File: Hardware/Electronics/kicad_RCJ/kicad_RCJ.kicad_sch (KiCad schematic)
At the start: 79 parts, among them J1 Raspberry_Pi_2_3, J10 Conn_01x04_M1_extra, J11 Conn_01x04_M2_extra, J12 Conn_01x04_M3_extra, J13 Conn_01x04_M4_extra, J14 Conn_01x06_teensy_left_extra, J15 Conn_01x04_teensy_right_extra, J16 Conn_01x07_IO_expander_extra, J17 Conn_02x03_I2C, J18 Conn_02x05_3V3_GND, J19 Conn_02x05_5V_GND, J2 Conn_01x06_IMU_extra, J20 Conn_01x06_BNO085_extra, J21 Conn_01x06_ISM20948_extra, J22 Conn_01x02_LSM5DSOX_LIS3MDL_e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, J23 VBAT_meas_conn, J24 Conn_01x02, J25 Conn_01x02, J26 Conn_01x02, J27 Conn_01x02, J28 Conn_01x02_5V, J29 Conn_01x02_3.3V, J3 Conn_01x02_colsens_interrupt, J4 Conn_01x02_5V, J5 Conn_01x02_3V3, J6 Conn_01x02_I2C1, J7 Conn_01x01_LOP, J8 Conn_01x03_IO_expander_interr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, J9 Conn_01x06_LED, M5 Servo1, M6 Servo2, U1 DRV8874, U12 VL53L0/1X, U13 VL53L0/1X, U14 VL53L0/1X, U15 VL53L0/1X, U16 VL53L0/1X, U17 VL53L0/1X, U18 VL53L0/1X, U2 DRV8874, U20 BNO085, U21 ICM20948, U22 LSM6DSOX+LIS3MDL, U23 TCS34725, U24 APDS9960, U25 VL53L0/1X, U3 DRV8874, U4 DRV8874

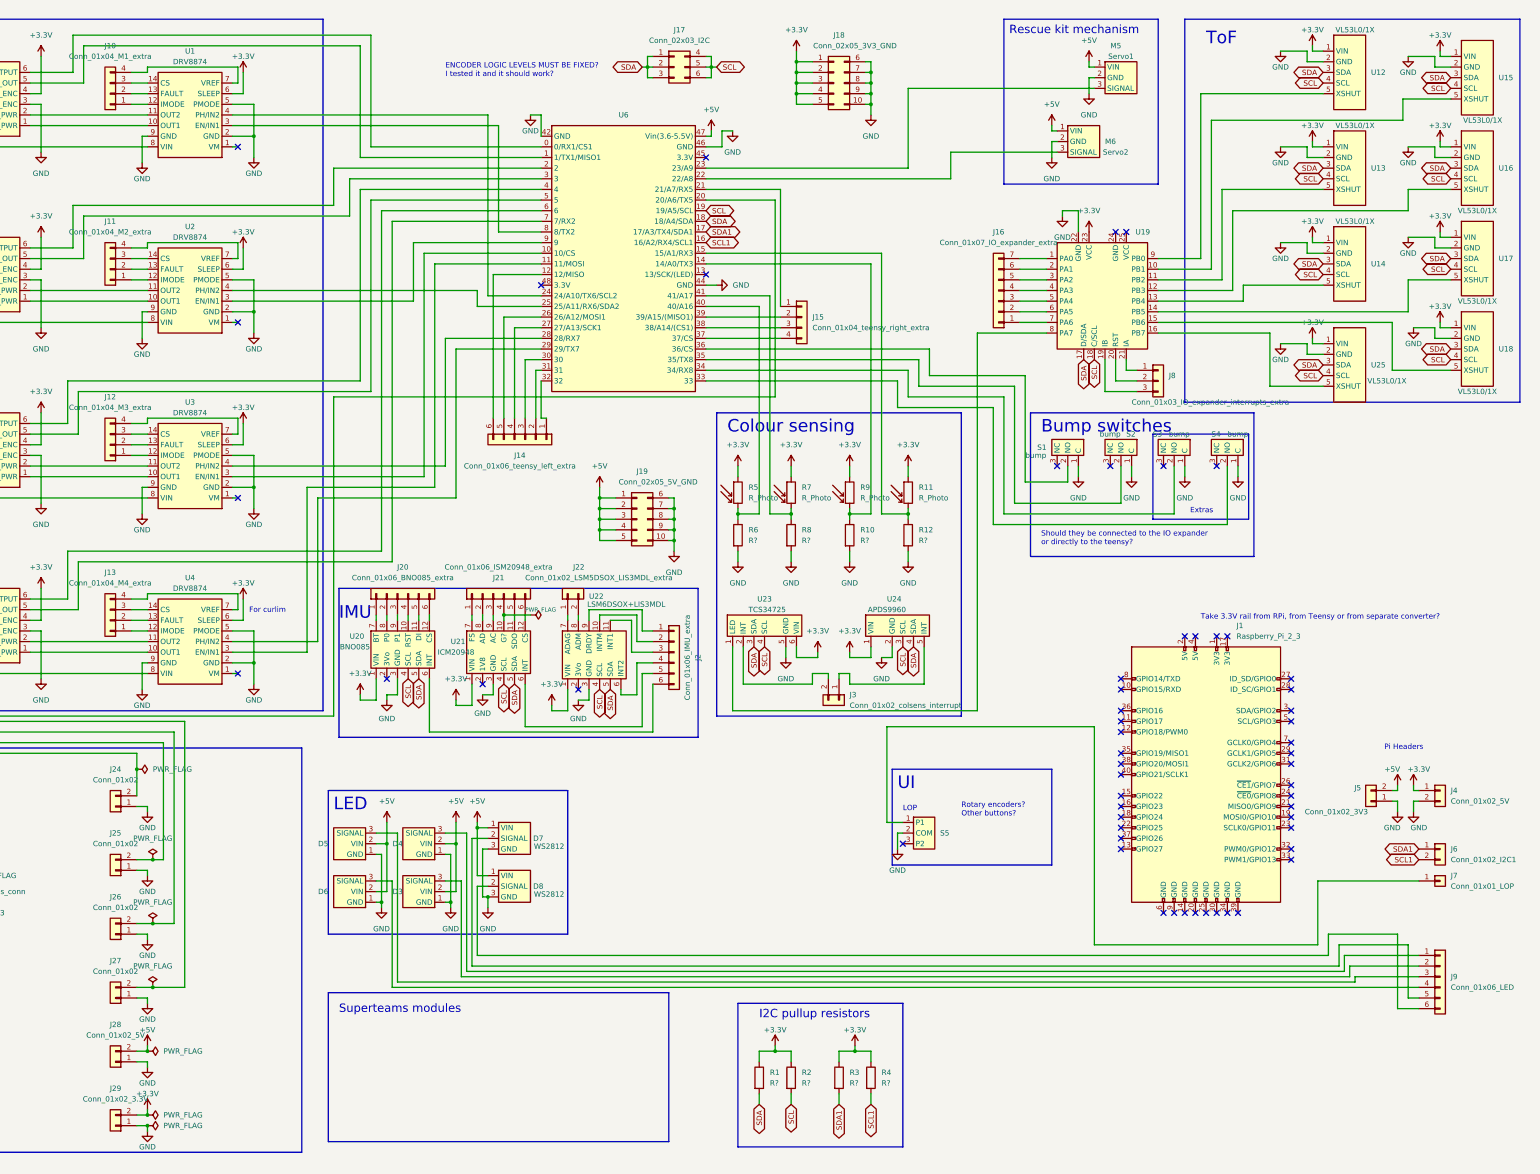
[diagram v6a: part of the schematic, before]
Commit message: enlarged PCB outline and rearranged
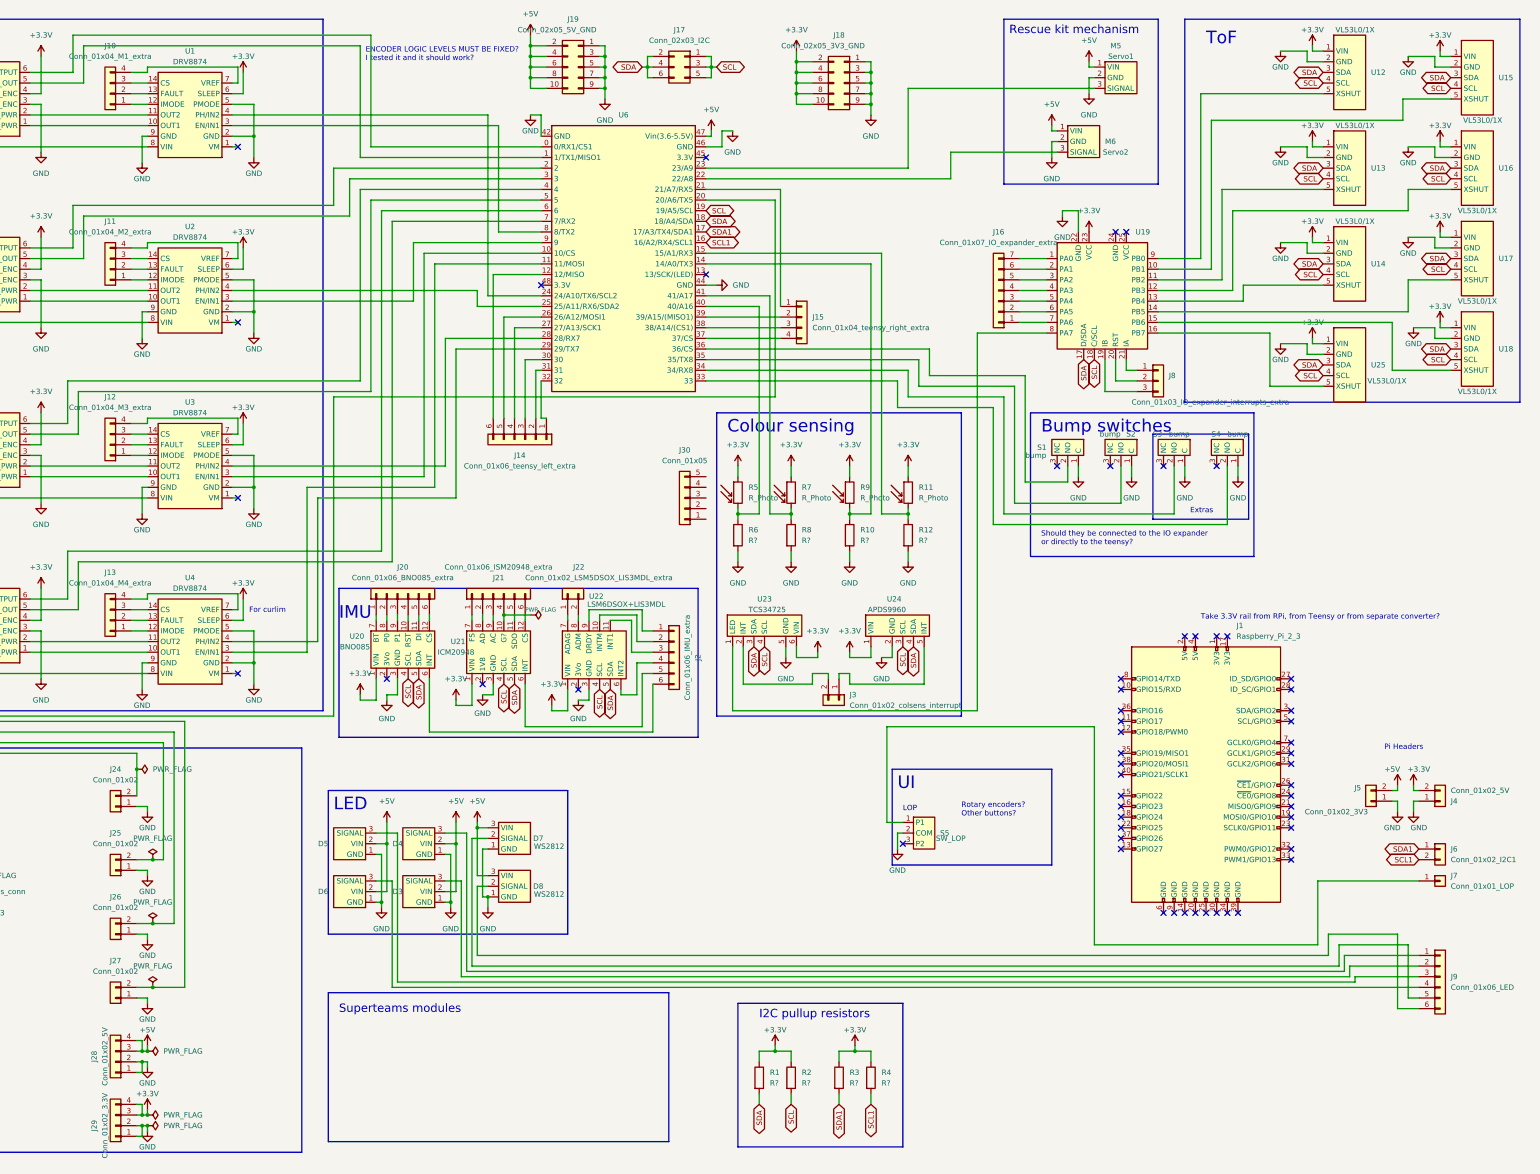
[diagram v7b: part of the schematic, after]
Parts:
- added J30: Conn_01x05, symbol Connector_Generic:Conn_01x05
- J17: symbol Connector_Generic:Conn_02x03_Top_Bottom -> Connector_Generic:Conn_02x03_Odd_Even
- J18, J19: symbol Connector_Generic:Conn_02x05_Top_Bottom -> Connector_Generic:Conn_02x05_Odd_Even
- J28, J29: footprint Connector_JST:JST_XH_B2B-XH-A_1x02_P2.50mm_Vertical -> Connector_JST:JST_XH_B4B-XH-A_1x04_P2.50mm_Vertical; symbol Connector_Generic:Conn_01x02 -> Connector_Generic:Conn_01x04
- S5: value ~ -> SW_LOP
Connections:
- net +3.3V: now also J18.10 (Pin_10), J18.6 (Pin_6), J18.8 (Pin_8), J29.3 (Pin_3), J29.4 (Pin_4), J4.2 (Pin_2); no longer J18.1 (Pin_1), J18.3 (Pin_3), J18.5 (Pin_5), J29.2 (Pin_2), J4.1 (Pin_1)
- net +5V: now also D7.3 (VIN), D8.3 (VIN), J19.10 (Pin_10), J19.6 (Pin_6), J19.8 (Pin_8), J28.3 (Pin_3), J28.4 (Pin_4); no longer D7.1 (VIN), D8.1 (VIN), J19.1 (Pin_1), J19.3 (Pin_3), J19.5 (Pin_5), J28.2 (Pin_2)
- net GND: now also D7.1 (GND), D8.1 (GND), J18.1 (Pin_1), J18.3 (Pin_3), J18.5 (Pin_5), J19.1 (Pin_1), J19.3 (Pin_3), J19.5 (Pin_5), J28.2 (Pin_2), J29.2 (Pin_2), J4.1 (Pin_1); no longer D7.3 (GND), D8.3 (GND), J18.10 (Pin_10), J18.6 (Pin_6), J18.8 (Pin_8), J19.10 (Pin_10), J19.6 (Pin_6), J19.8 (Pin_8), J4.2 (Pin_2)
- net SCL: now also J17.1 (Pin_1), J17.3 (Pin_3); no longer J17.4 (Pin_4), J17.6 (Pin_6)
- net SDA: now also J17.4 (Pin_4), J17.6 (Pin_6); no longer J17.1 (Pin_1), J17.3 (Pin_3)
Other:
- moved on the sheet: J19

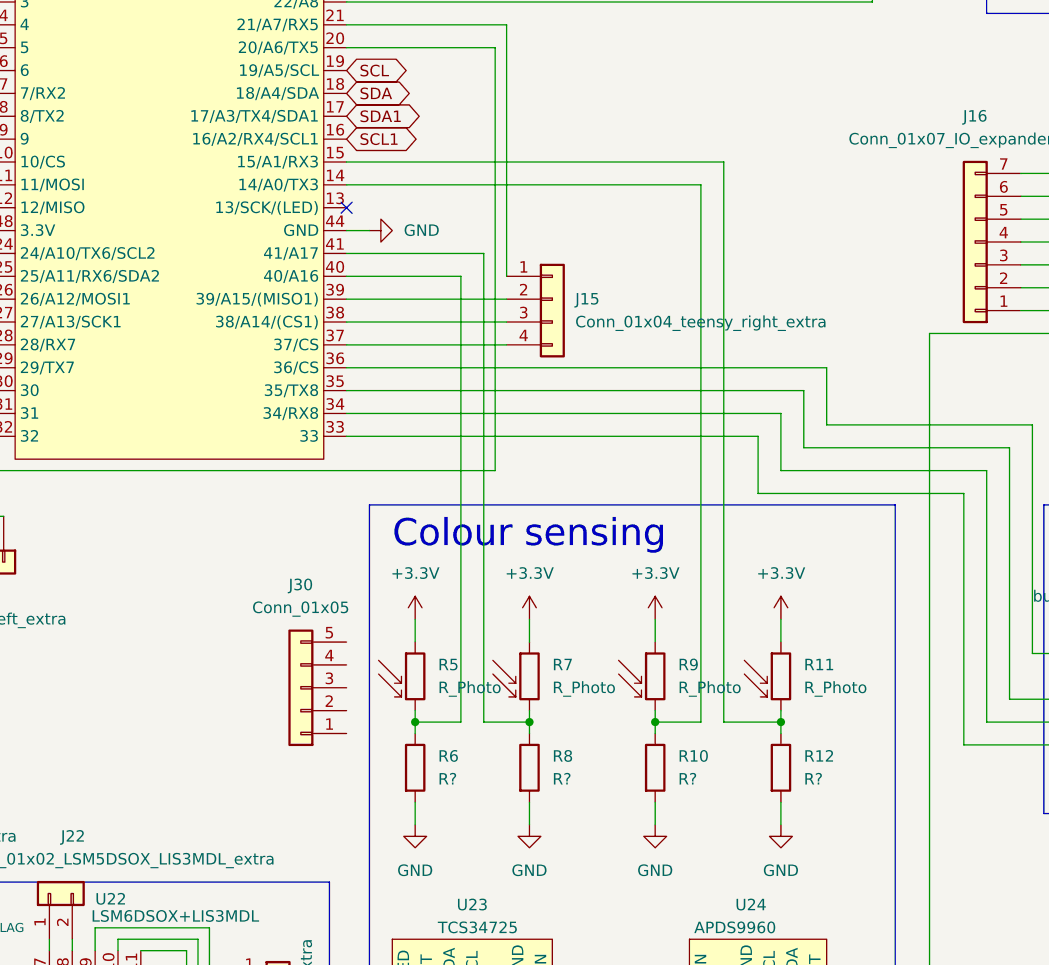
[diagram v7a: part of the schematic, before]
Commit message: increased component spacing and fixed custom footprints
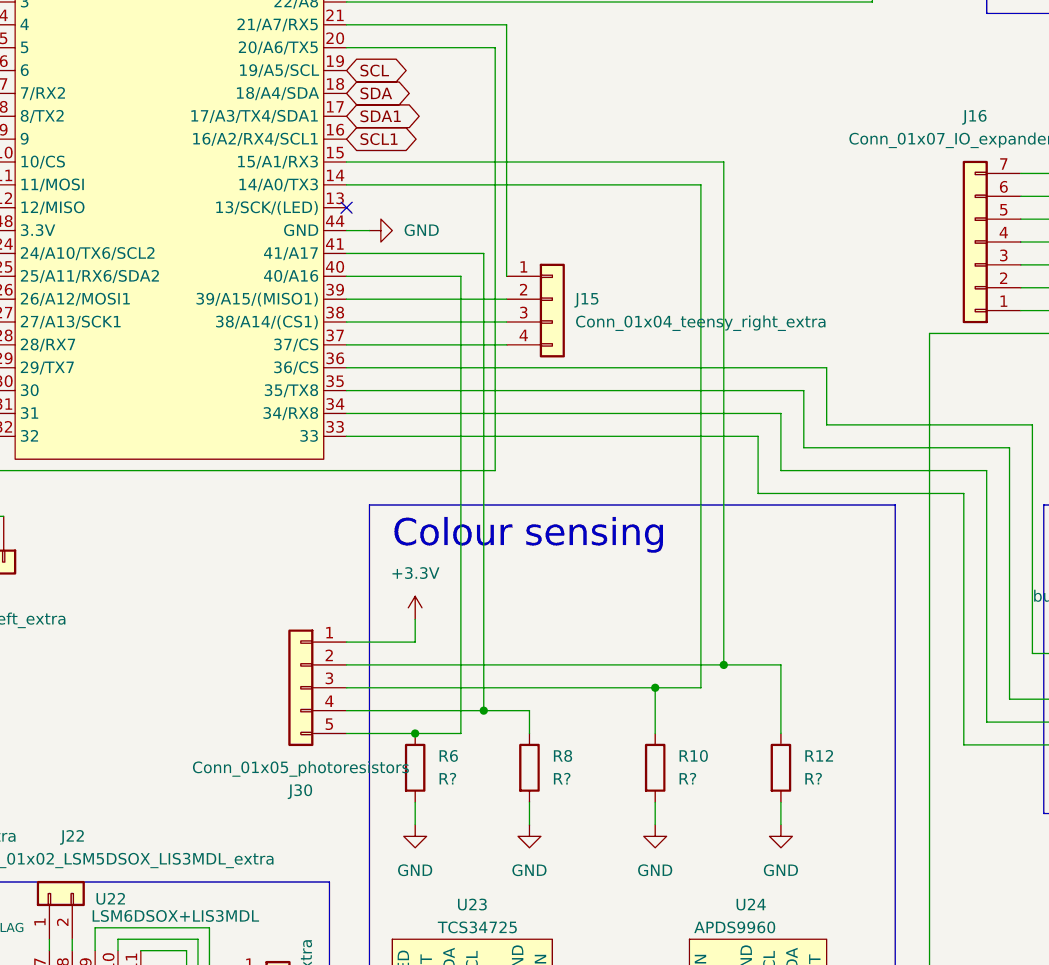
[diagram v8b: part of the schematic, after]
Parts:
- removed R11, R5, R7, R9: R_Photo, Connector_JST:JST_XH_B2B-XH-A_1x02_P2.50mm_Vertical, symbol Device:R_Photo
- J30: value Conn_01x05 -> Conn_01x05_photoresistors; footprint (none) -> Connector_JST:JST_XH_B5B-XH-A_1x05_P2.50mm_Vertical
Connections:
- net +3.3V: now also J30.1 (Pin_1)
- net at R10.1, U6.14 (14/A0/TX3): now also J30.3 (Pin_3)
- net at R6.1, U6.40 (40/A16): now also J30.5 (Pin_5)
- net at R12.1, U6.15 (15/A1/RX3): now also J30.2 (Pin_2)
- net at J30.4 (Pin_4): now also R8.1, U6.41 (41/A17)
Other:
- moved on the sheet: J30
